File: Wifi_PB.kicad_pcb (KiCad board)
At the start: 2 copper layers, 100 x 49.7 mm, 197 parts, among them P1 CONN_01X02, P10 CONN_01X01, P12 CONN_01X04, P13 CONN_01X04, P14 CONN_01X04, P15 USB_MINI, P16 CONN_01X01, P17 CONN_01X01, P18 CONN_01X01, P19 CONN_01X01, P2 CONN_01X03, P3 CONN_01X03, P4 CONN_01X03, P5 CONN_01X03, P6 CONN_01X01, P7 CONN_01X01, P8 CONN_01X01, P9 CONN_01X01, Q1 SMBT3904, Q10 BC849, Q11 NX2301P, Q2 SMBT3904, Q3 BSS138, Q4 BSS138, Q5 SMBT3904, Q6 SMBT3904, Q7 SMBT3904, Q8 SMBT3904, Q9 SMBT3904, SW1 Pulsador_2p, SW2 Pulsador_2p, SW3 Pulsador_2p, SW4 Pulsador_2p, U1 MCP73831T, U10 Matriz_5x7_Anodo_Filas, U11 40106, U12 MCP1640, U2 LD1117S33TR, U3 CH340G, U4 ESP8266, U5 MMA7660FC, U6 MCP23017, U7 MCP23017, U8 MCP3204, U9 PCA9551, Y1 Cristal

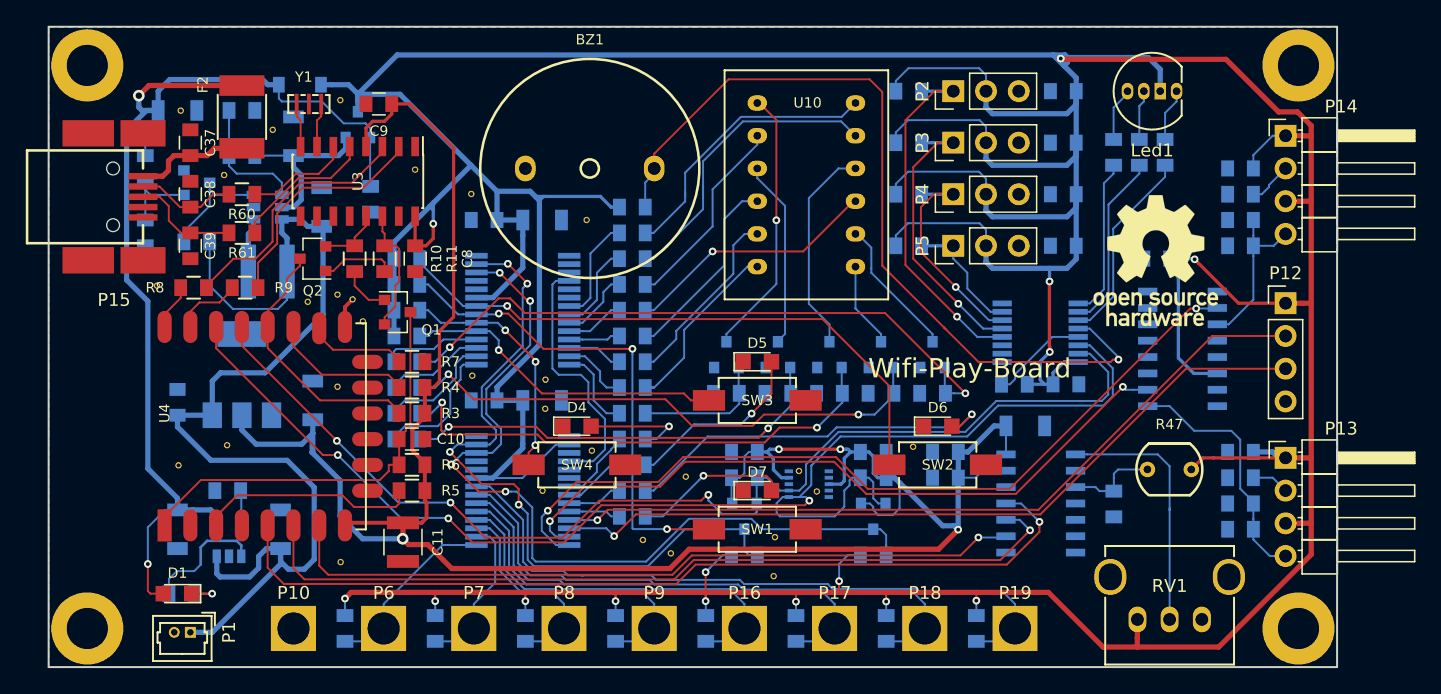
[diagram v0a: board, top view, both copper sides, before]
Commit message: conectar reset gpio. retocar plano masa
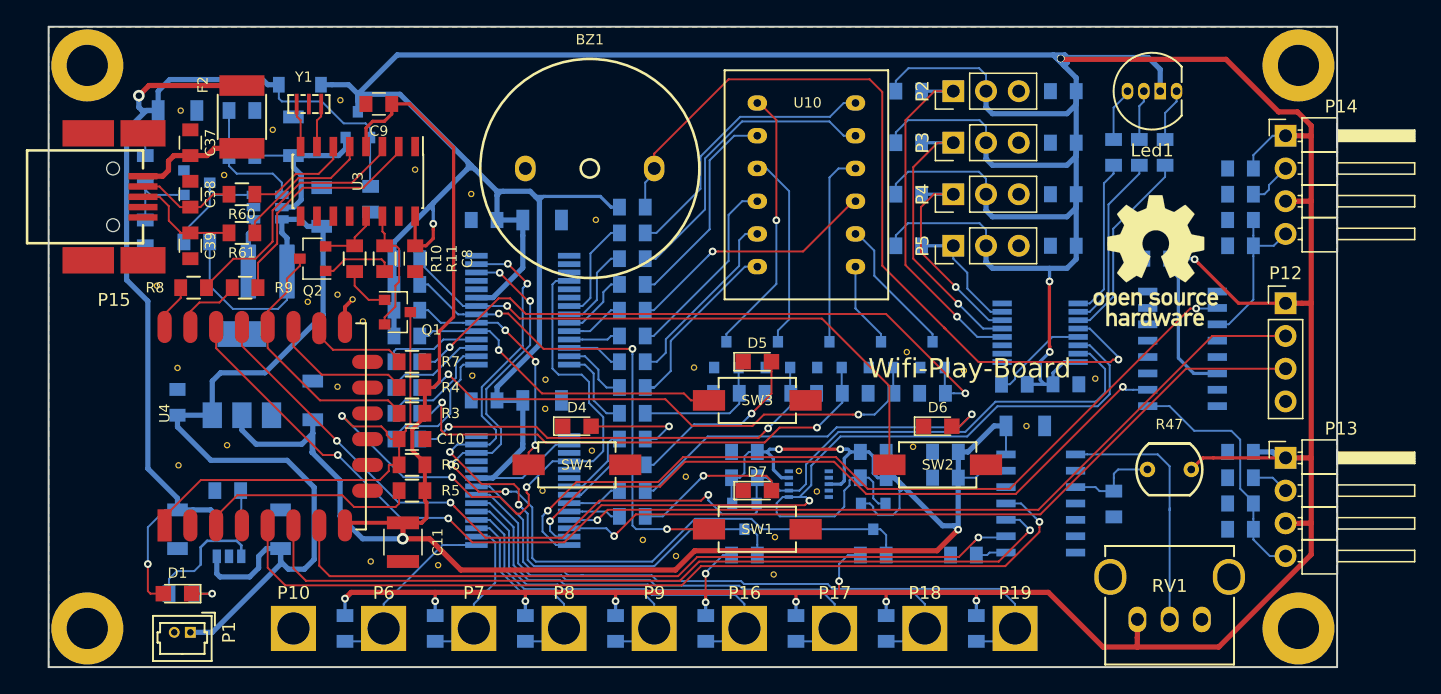
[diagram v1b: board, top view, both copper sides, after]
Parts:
- added Gnd-Via: VAL**, Vias:Gnd-Via, F.Cu at (125.0, 61.7)
- added Gnd-Via: VAL**, Vias:Gnd-Via, F.Cu at (120.6, 60.2)
- added Gnd-Via: VAL**, Vias:Gnd-Via, F.Cu at (104.1, 61.5)
- added Gnd-Via: VAL**, Vias:Gnd-Via, F.Cu at (135.2, 62.3)
- added Gnd-Via: VAL**, Vias:Gnd-Via, F.Cu at (129.9, 66.0)
- added Gnd-Via: VAL**, Vias:Gnd-Via, F.Cu at (84.2, 76.8)
- added Gnd-Via: VAL**, Vias:Gnd-Via, F.Cu at (64.0, 61.5)
- added R72: 47K, Resistencias:R_0805, B.Cu at (125.0, 76.0)
- moved Gnd-Via 2.34 mm to (79.0, 76.5)
- moved Gnd-Via 0.72 mm to (96.5, 50.0)
- moved Gnd-Via 0.45 mm to (102.7, 76.1)
- moved Gnd-Via 0.13 mm to (110.3, 77.5)
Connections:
- net CH1 renamed Net-(U8-Pad2)
- net CH3 renamed Net-(U8-Pad4)
- net D3 renamed Net-(U5-Pad5)
- C10 pad 1: /Control/~RST -> ~RESET
- Q1 pad 3: /Control/~RST -> ~RESET
- R6 pad 1: /Control/~RST -> ~RESET
- U4 pad 1: /Control/~RST -> ~RESET
- U8 pad 8: AD_NSS -> Net-(R72-Pad1)
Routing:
- net ~RESET: track 20.1 -> 81.2 mm, vias 0 -> 3
- net /Control/~RST: track 32.4 -> 0.00 mm
- net Net-(R72-Pad1): track 0.00 -> 2.38 mm
- net +5V: track 481.4 -> 483.3 mm
- net Net-(Q7-Pad3): track 16.4 -> 15.1 mm
- net +3V3: track 171.7 -> 172.9 mm
- net Net-(R32-Pad1): track 15.9 -> 17.0 mm
- net Net-(R26-Pad1): track 24.4 -> 23.5 mm
- net Net-(Q6-Pad3): track 14.6 -> 15.2 mm
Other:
- board text added: "02/17"
- board text added: "V0.1"

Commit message: girar conector detector ultrasionidos
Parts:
- moved P12 7.64 mm to (150.0, 64.1), turned to 180 degrees
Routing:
- net +5V: track 483.3 -> 505.0 mm
- net PC5: track 61.2 -> 62.7 mm
- net VBATT: track 84.7 -> 85.9 mm
- net VUSB: track 87.3 -> 88.5 mm
- net +3V3: track 172.9 -> 173.5 mm
- net PC4: track 61.5 -> 62.1 mm
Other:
- board text added: "E+"
- board text added: "E-"
- board text added: "R+"
- board text added: "R-"
- board text added: "SERVO"

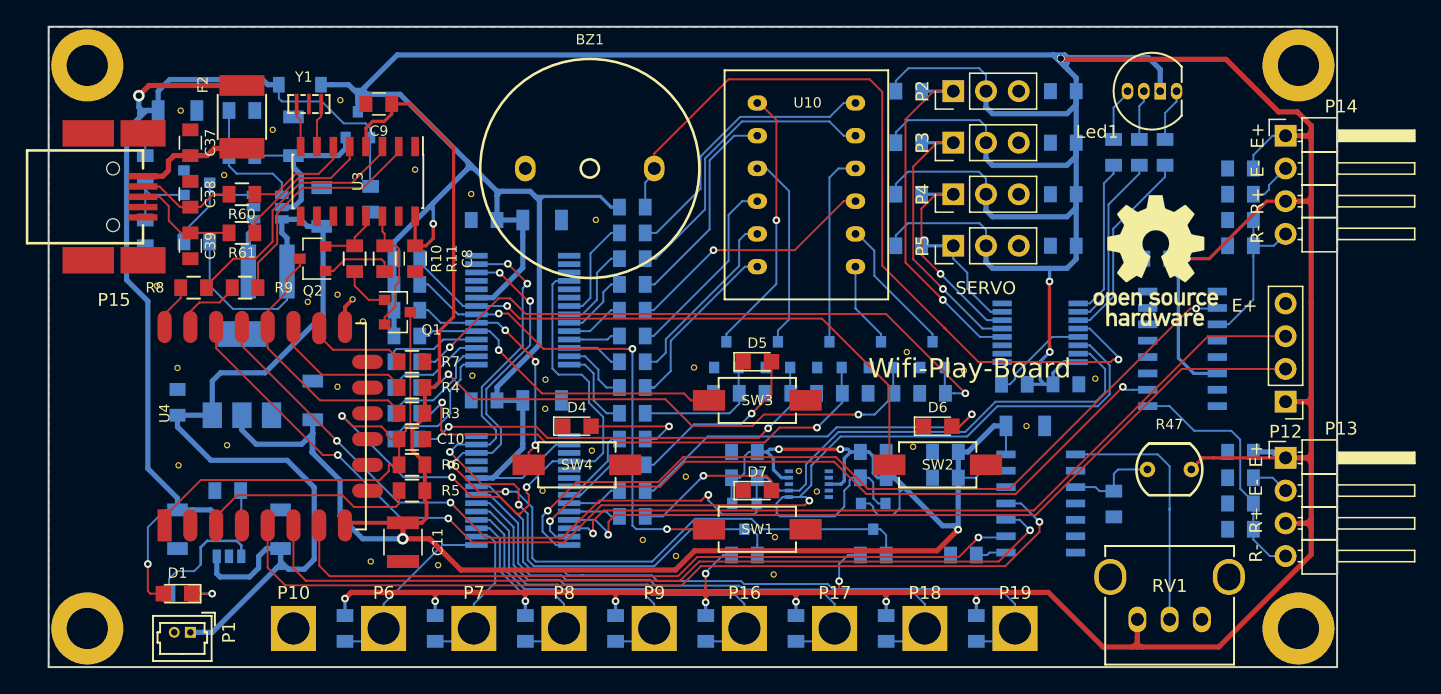
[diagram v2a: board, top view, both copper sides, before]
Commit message: Mejoras en serigrafia
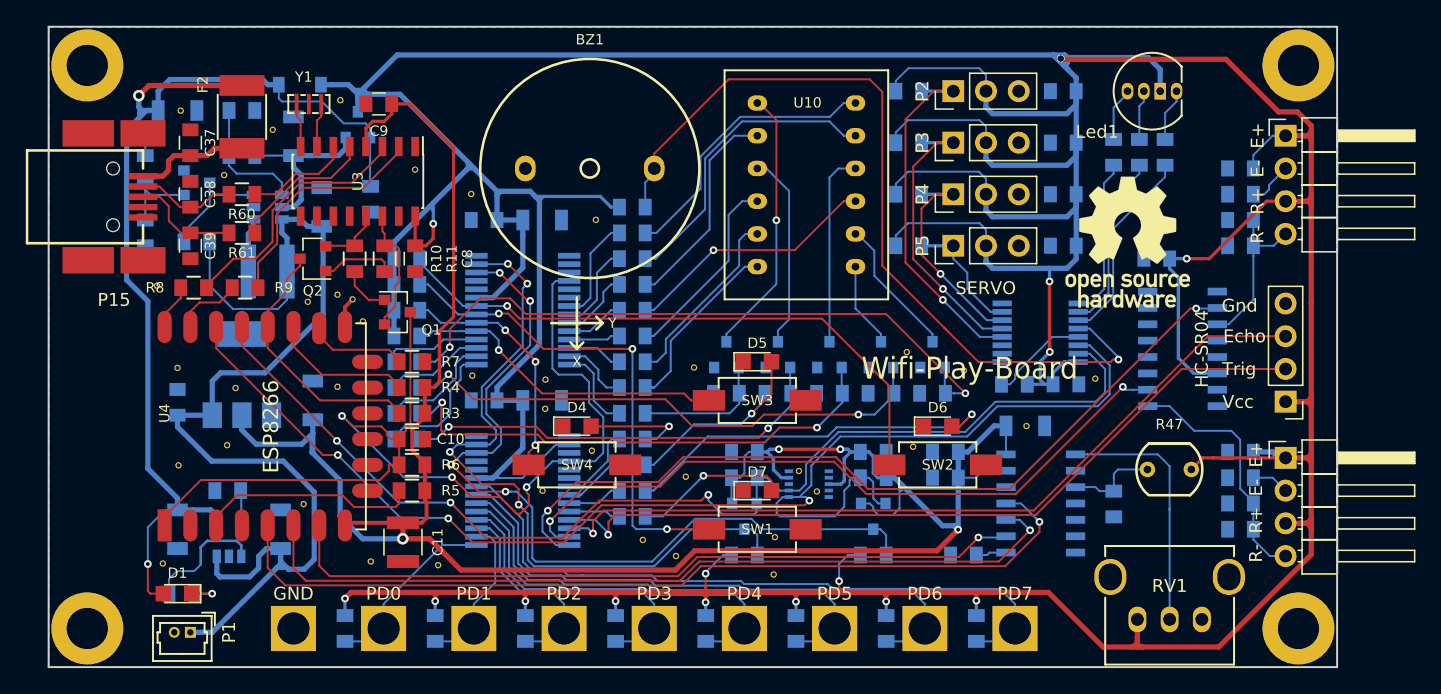
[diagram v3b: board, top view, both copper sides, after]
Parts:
- added Gnd-Via: VAL**, Vias:Gnd-Via, F.Cu at (68.5, 63.0)
- added Gnd-Via: VAL**, Vias:Gnd-Via, F.Cu at (62.9, 76.7)
- added Gnd-Via: VAL**, Vias:Gnd-Via, F.Cu at (73.8, 72.0)
- moved G*** 2.61 mm to (137.7, 51.7)
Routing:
- net Net-(Q9-Pad1): track 51.0 -> 51.8 mm
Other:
- board text added: "ESP8266"
- board text added: "Echo"
- board text added: "GND"
- board text added: "Gnd"
- board text added: "HC-SR04"
- board text added: "PD0"
- board text added: "PD1"
- board text added: "PD2"
- board text added: "PD3"
- board text added: "PD4"
- board text added: "PD5"
- board text added: "PD6"
- board text added: "PD7"
- board text added: "Trig"
- board text added: "Vcc"
- board text added: "X"
- board text added: "Y"

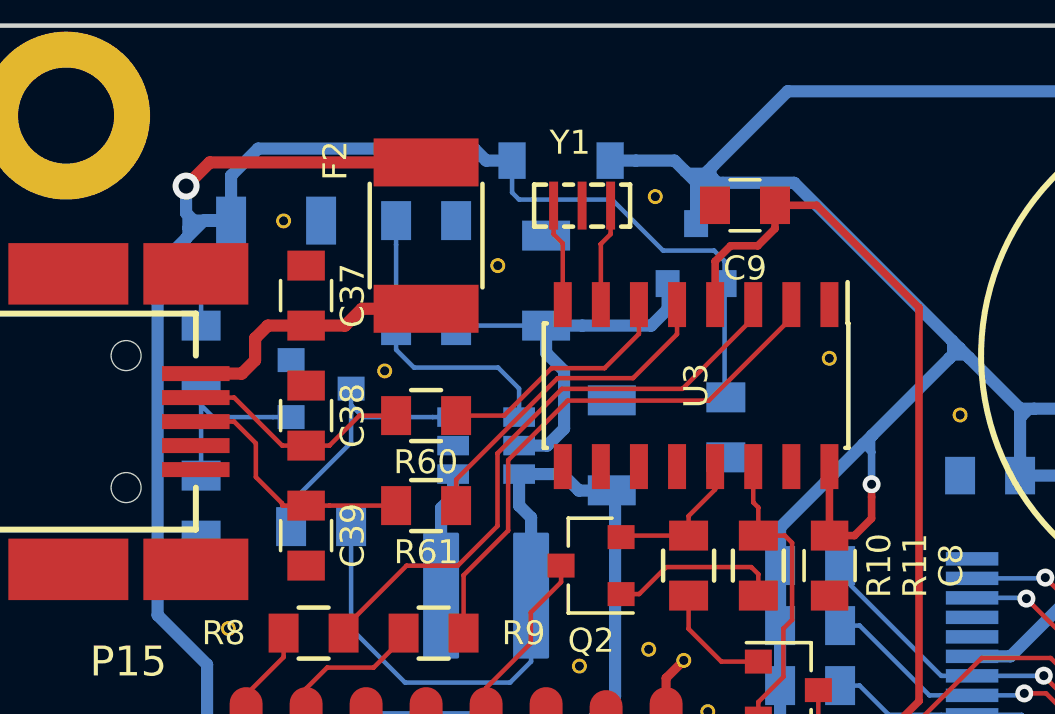
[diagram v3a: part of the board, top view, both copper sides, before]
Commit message: finalizada pcb V0.1
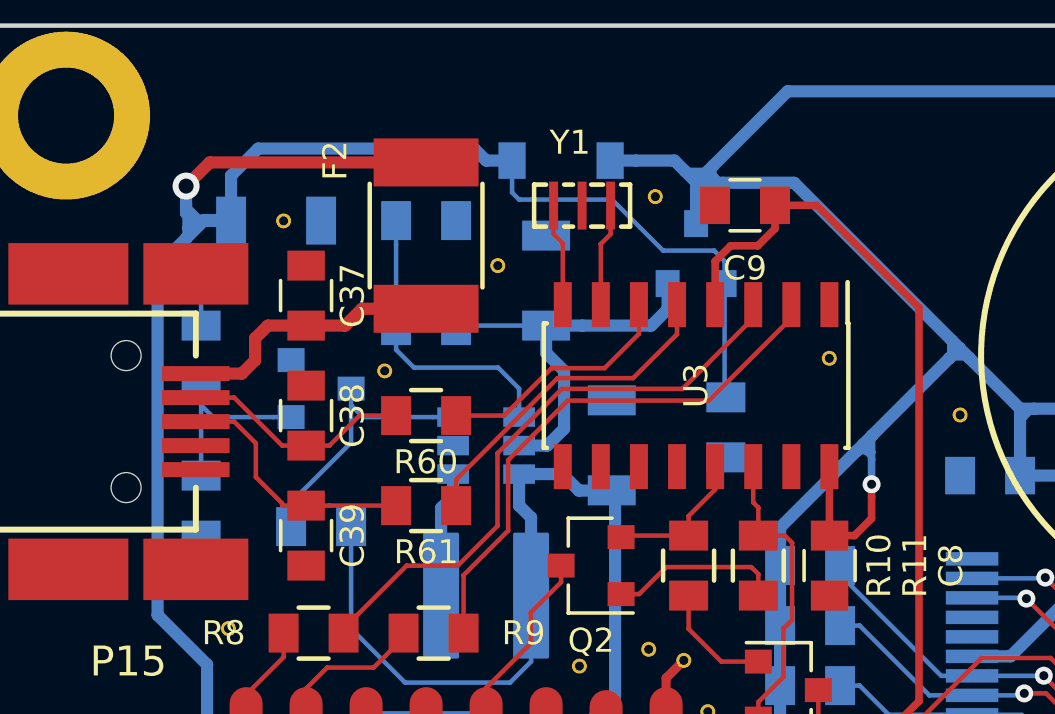
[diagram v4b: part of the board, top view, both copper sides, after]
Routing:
- net +5V: track 505.0 -> 505.8 mm
- net VUSB: track 88.5 -> 89.3 mm
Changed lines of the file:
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@@
 (kicad_pcb (version 20170123) (host pcbnew no-vcs-found-7650~57~ubuntu14.04.1)
   (general
-    (links 387)
+    (links 388)
     (no_connects 0)
     (area 53.924999 34.924999 154.075001 84.775001)
     (thickness 1.6)
     (drawings 45)
-    (tracks 1573)
+    (tracks 1584)
     (zones 0)
     (modules 208)
@@
   (segment (start 77 59) (end 77 56.75) (width 0.3048) (layer F.Cu) (net 2))
   (segment (start 77 56.75) (end 77.59 56.16) (width 0.3048) (layer F.Cu) (net 2))
+  (segment (start 60.05 43.0436) (end 61.01 42.0836) (width 0.4064) (layer B.Cu) (net 3))
+  (segment (start 61 40.95) (end 61 41.25) (width 0.4064) (layer B.Cu) (net 3))
+  (segment (start 61.56 41.5) (end 62.5 41.5) (width 0.4064) (layer B.Cu) (net 3))
+  (segment (start 61 40.35) (end 61 40.95) (width 0.4064) (layer B.Cu) (net 3))
+  (segment (start 61.25 41.5) (end 61.56 41.5) (width 0.4064) (layer B.Cu) (net 3))
+  (segment (start 61 40.95) (end 61.01 40.95) (width 0.1524) (layer B.Cu) (net 3))
+  (segment (start 61.01 40.95) (end 61.56 41.5) (width 0.1524) (layer B.Cu) (net 3))
   (segment (start 61 41.25) (end 61 41.74) (width 0.254) (layer B.Cu) (net 3))
   (segment (start 61 41.74) (end 61 42.0736) (width 0.254) (layer B.Cu) (net 3))
   (segment (start 61.25 41.5) (end 61.24 41.5) (width 0.254) (layer B.Cu) (net 3))
   (segment (start 61.24 41.5) (end 61 41.74) (width 0.254) (layer B.Cu) (net 3))
-  (segment (start 60.05 43.0436) (end 61.01 42.0836) (width 0.4064) (layer B.Cu) (net 3))
   (segment (start 61.01 42.0836) (end 61.5936 41.5) (width 0.4064) (layer B.Cu) (net 3))
   (segment (start 61 42.0736) (end 61.01 42.0836) (width 0.254) (layer B.Cu) (net 3))
@@
   (segment (start 61.5936 41.5) (end 62.5 41.5) (width 0.4064) (layer B.Cu) (net 3))
   (segment (start 61 41.25) (end 61.25 41.5) (width 0.4064) (layer B.Cu) (net 3))
-  (segment (start 61.25 41.5) (end 62.5 41.5) (width 0.4064) (layer B.Cu) (net 3))
-  (segment (start 61 40.35) (end 61 41.25) (width 0.4064) (layer B.Cu) (net 3))
   (segment (start 61.7884 39.5616) (end 61 40.35) (width 0.4064) (layer F.Cu) (net 3))
   (via (at 61 40.35) (size 0.9) (drill 0.5) (layers F.Cu B.Cu) (net 3))
@@
   (segment (start 81.5 73.5) (end 77.5 73.5) (width 0.3048) (layer F.Cu) (net 5))
   (segment (start 77.5 73.5) (end 77 73) (width 0.3048) (layer F.Cu) (net 5))
+  (segment (start 83.85 49.46) (end 83.85 49.22) (width 0.254) (layer B.Cu) (net 6))
+  (segment (start 83.85 50.29) (end 83.85 49.46) (width 0.254) (layer B.Cu) (net 6))
+  (segment (start 83.65 49.22) (end 83.39 49.22) (width 0.1524) (layer B.Cu) (net 6))
+  (segment (start 83.85 49.22) (end 83.65 49.22) (width 0.1524) (layer B.Cu) (net 6))
+  (segment (start 83.85 49.46) (end 83.85 49.42) (width 0.1524) (layer B.Cu) (net 6))
+  (segment (start 83.85 49.42) (end 83.65 49.22) (width 0.1524) (layer B.Cu) (net 6))
+  (segment (start 80.8 51.73) (end 83.35 49.18) (width 0.4064) (layer B.Cu) (net 6))
+  (segment (start 83.39 49.22) (end 83.35 49.18) (width 0.1524) (layer B.Cu) (net 6))
+  (segment (start 83.35 49.18) (end 83.58 48.95) (width 0.4064) (layer B.Cu) (net 6))
   (segment (start 84 78.9) (end 83.66 78.9) (width 0.4064) (layer F.Cu) (net 6))
   (segment (start 83.66 78.9) (end 77.48 78.9) (width 0.4064) (layer F.Cu) (net 6))
@@
   (segment (start 83.85 49.22) (end 83.85 48.68) (width 0.254) (layer B.Cu) (net 6))
   (segment (start 83.85 48.68) (end 83.87 48.66) (width 0.254) (layer B.Cu) (net 6))
-  (segment (start 80.8 51.73) (end 83.58 48.95) (width 0.4064) (layer B.Cu) (net 6))
-  (segment (start 83.85 50.29) (end 83.85 49.22) (width 0.254) (layer B.Cu) (net 6))
   (segment (start 83.85 49.22) (end 83.58 48.95) (width 0.254) (layer B.Cu) (net 6))
   (segment (start 82.45 52) (end 83.28 52) (width 0.254) (layer F.Cu) (net 6))

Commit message: ajustada margen mascara soldadura a 5 mils
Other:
- rule pad_to_mask_clearance: 0.2 -> 0.127
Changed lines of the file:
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@@
     (mod_text_size 1 1)
     (mod_text_width 0.15)
-    (pad_size 0.5 0.5)
-    (pad_drill 0.3)
-    (pad_to_mask_clearance 0.2)
+    (pad_size 5.6 5.6)
+    (pad_drill 3.2)
+    (pad_to_mask_clearance 0.127)
     (aux_axis_origin 0 0)
     (visible_elements FFFFFF7F)
@@
     (fp_circle (center 0 0) (end 3.05 0) (layer F.CrtYd) (width 0.05))
     (fp_circle (center 0 0) (end 2.8 0) (layer Cmts.User) (width 0.15))
-    (pad 1 thru_hole circle (at 0 0) (size 5.6 5.6) (drill 3.2) (layers *.Cu *.Mask))
+    (pad 1 thru_hole circle (at 0 0) (size 5.6 5.6) (drill 3.2) (layers *.Cu))
   )
   (module Mounting_Holes:MountingHole_3.2mm_M3_DIN965_Pad (layer F.Cu)
@@
     (fp_circle (center 0 0) (end 2.8 0) (layer Cmts.User) (width 0.15))
     (fp_circle (center 0 0) (end 3.05 0) (layer F.CrtYd) (width 0.05))
-    (pad 1 thru_hole circle (at 0 0) (size 5.6 5.6) (drill 3.2) (layers *.Cu *.Mask))
+    (pad 1 thru_hole circle (at 0 0) (size 5.6 5.6) (drill 3.2) (layers *.Cu))
   )
   (module Mounting_Holes:MountingHole_3.2mm_M3_DIN965_Pad (layer F.Cu)
@@
     (fp_circle (center 0 0) (end 3.05 0) (layer F.CrtYd) (width 0.05))
     (fp_circle (center 0 0) (end 2.8 0) (layer Cmts.User) (width 0.15))
-    (pad 1 thru_hole circle (at 0 0) (size 5.6 5.6) (drill 3.2) (layers *.Cu *.Mask))
+    (pad 1 thru_hole circle (at 0 0) (size 5.6 5.6) (drill 3.2) (layers *.Cu))
   )
   (module Mounting_Holes:MountingHole_3.2mm_M3_DIN965_Pad (layer F.Cu)
@@
     (fp_circle (center 0 0) (end 2.8 0) (layer Cmts.User) (width 0.15))
     (fp_circle (center 0 0) (end 3.05 0) (layer F.CrtYd) (width 0.05))
-    (pad 1 thru_hole circle (at 0 0) (size 5.6 5.6) (drill 3.2) (layers *.Cu *.Mask))
+    (pad 1 thru_hole circle (at 0 0) (size 5.6 5.6) (drill 3.2) (layers *.Cu))
   )
   (module Buzzer:LOUDITY_LD-BZPN-1705 (layer F.Cu)
